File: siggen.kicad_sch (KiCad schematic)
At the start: 0 parts

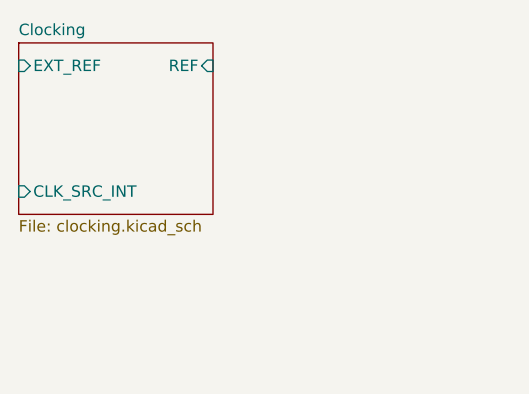
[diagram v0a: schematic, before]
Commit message: Added PLL1, entered in MPNs of all parts
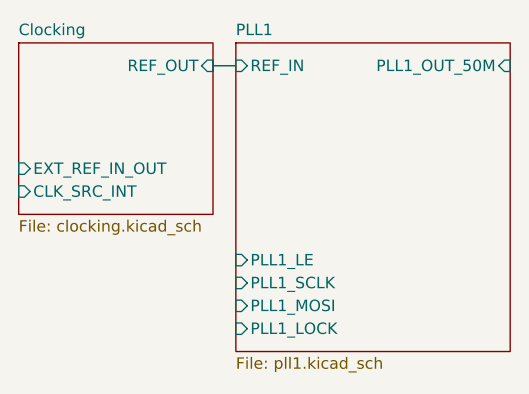
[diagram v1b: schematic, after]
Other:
- added sheet PLL1 (pll1.kicad_sch)
- sheet Clocking ports: added EXT_REF_IN_OUT, REF_OUT; removed EXT_REF, REF
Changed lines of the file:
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@@
 	(generator_version "8.0")
 	(paper "B")
+	(wire
+		(pts
+			(xy 66.04 88.9) (xy 68.58 88.9)
+		)
+		(stroke
+			(width 0)
+			(type default)
+		)
+	)
 	(sheet
 		(at 44.45 86.36)
@@
 			)
 		)
-		(pin "EXT_REF" input
-			(at 44.45 88.9 180)
-			(effects
-				(font
-					(size 1.27 1.27)
-				)
-				(justify left)
-			)
-		)
 		(pin "CLK_SRC_INT" input
 			(at 44.45 102.87 180)
@@
 			)
 		)
-		(pin "REF" input
+		(pin "REF_OUT" input
 			(at 66.04 88.9 0)
 			(effects
@@
 			)
 		)
+		(pin "EXT_REF_IN_OUT" input
+			(at 44.45 100.33 180)
+			(effects
+				(font
+					(size 1.27 1.27)
+				)
+				(justify left)
+			)
+		)
 		(instances
 			(project "siggen"
@@
 				)
 			)
+		)
+	)
+	(sheet
+		(at 68.58 86.36)
+		(size 30.48 34.29)
+		(fields_autoplaced yes)
+		(stroke
+			(width 0.1524)
+			(type solid)
+		)
+		(fill
+			(color 0 0 0 0.0000)
+		)
+		(property "Sheetname" "PLL1"
+			(at 68.58 85.6484 0)
+			(effects
+				(font
+					(size 1.27 1.27)
+				)
+				(justify left bottom)
+			)
+		)
+		(property "Sheetfile" "pll1.kicad_sch"
+			(at 68.58 121.2346 0)
+			(effects
+				(font
+					(size 1.27 1.27)
+				)
+				(justify left top)
+			)
+		)
+		(pin "PLL1_OUT_50M" input
+			(at 99.06 88.9 0)
+			(effects
+				(font
+					(size 1.27 1.27)
+				)
+				(justify right)
+			)
+		)
+		(pin "PLL1_LE" input
+			(at 68.58 110.49 180)
+			(effects
+				(font
+					(size 1.27 1.27)
+				)
+				(justify left)
+			)
+		)
+		(pin "PLL1_SCLK" input
+			(at 68.58 113.03 180)
+			(effects
+				(font
+					(size 1.27 1.27)
+				)
+				(justify left)
+			)
+		)
+		(pin "PLL1_MOSI" input
+			(at 68.58 115.57 180)
+			(effects
+				(font
+					(size 1.27 1.27)
+				)
+				(justify left)
+			)
+		)
+		(pin "REF_IN" input
+			(at 68.58 88.9 180)
+			(effects
+				(font
+					(size 1.27 1.27)
+				)
+				(justify left)
+			)
+		)
+		(pin "PLL1_LOCK" input
+			(at 68.58 118.11 180)
+			(effects
+				(font
+					(size 1.27 1.27)
+				)
+				(justify left)
+			)
+		)
+		(instances
+			(project "siggen"
+				(path "/49f19363-9055-4ac9-9bec-b181bee16fd6"
+					(page "3")
+				)
+			)
